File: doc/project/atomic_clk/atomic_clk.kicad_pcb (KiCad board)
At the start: 2 copper layers, 47.8 x 30.2 mm, 22 parts, among them J1 Goldpin, J2 Bat, SW1 POWER, SW2 SET, SW3 CLEAR, U1 BQ-M322RD, U2 STM32F030F4Px, U3 TC1185-3.3VCT8, Y1 18.432MHz

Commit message: better pathm replaced uc
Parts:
- moved U2 9.32 mm to (219.7, 113.5)
- turned R9 to 270 degrees
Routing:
- net D1: track 54.2 -> 24.2 mm
- net D4: track 11.2 -> 38.0 mm, vias 1 -> 0
- net GND: track 97.9 -> 111.3 mm
- net SE: track 32.6 -> 20.3 mm
- net Net-(R8-Pad1): track 37.6 -> 27.9 mm
- net Net-(R9-Pad2): track 30.5 -> 21.3 mm
- net Net-(C1-Pad1): track 19.8 -> 12.0 mm
- net SF: track 42.6 -> 35.7 mm
- net D2: track 23.6 -> 29.9 mm, vias 2 -> 1
- net Net-(C2-Pad1): track 22.5 -> 16.2 mm
- net SB: track 15.1 -> 21.4 mm
- net Net-(SW2-Pad1): track 20.4 -> 14.4 mm
- net SC: track 13.3 -> 19.3 mm
- net SD: track 18.2 -> 12.9 mm
- net +3V3: track 54.3 -> 59.6 mm, vias 2 -> 0
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
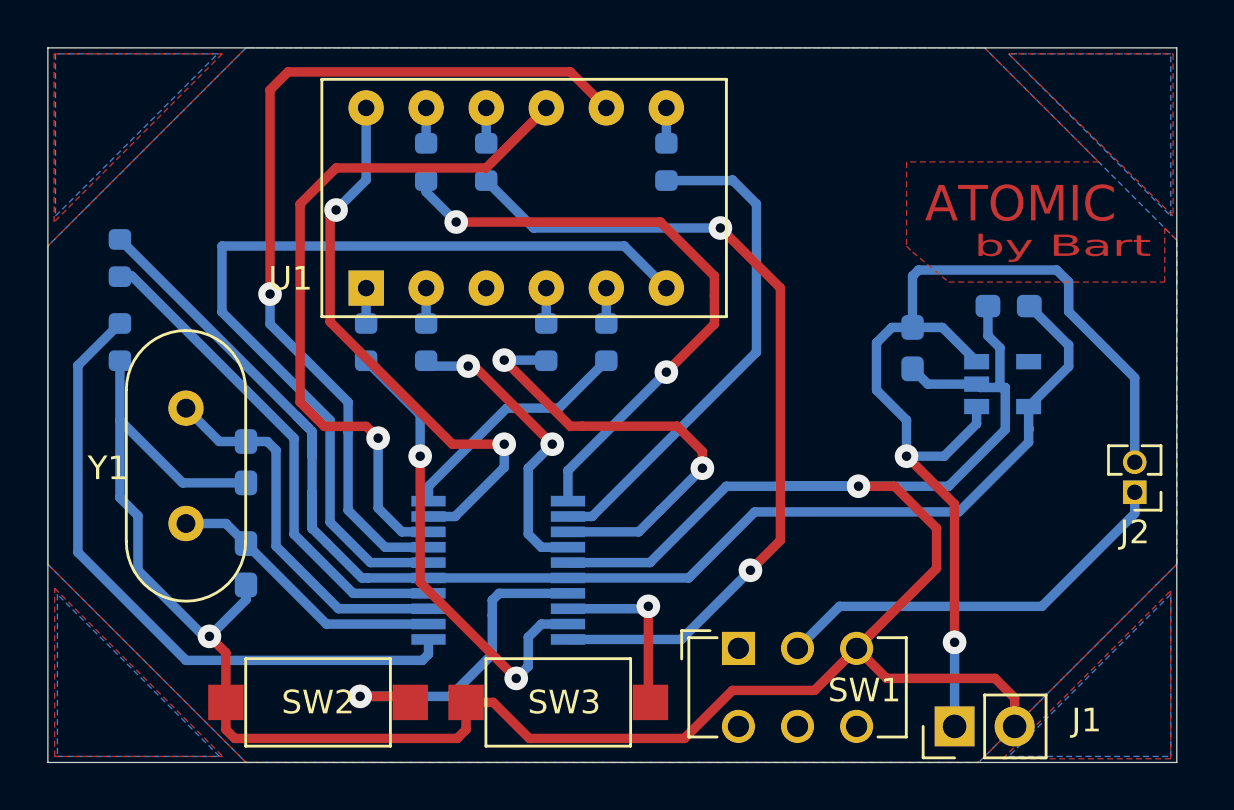
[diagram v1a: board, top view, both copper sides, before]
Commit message: zminimalizowana ilość przelotek
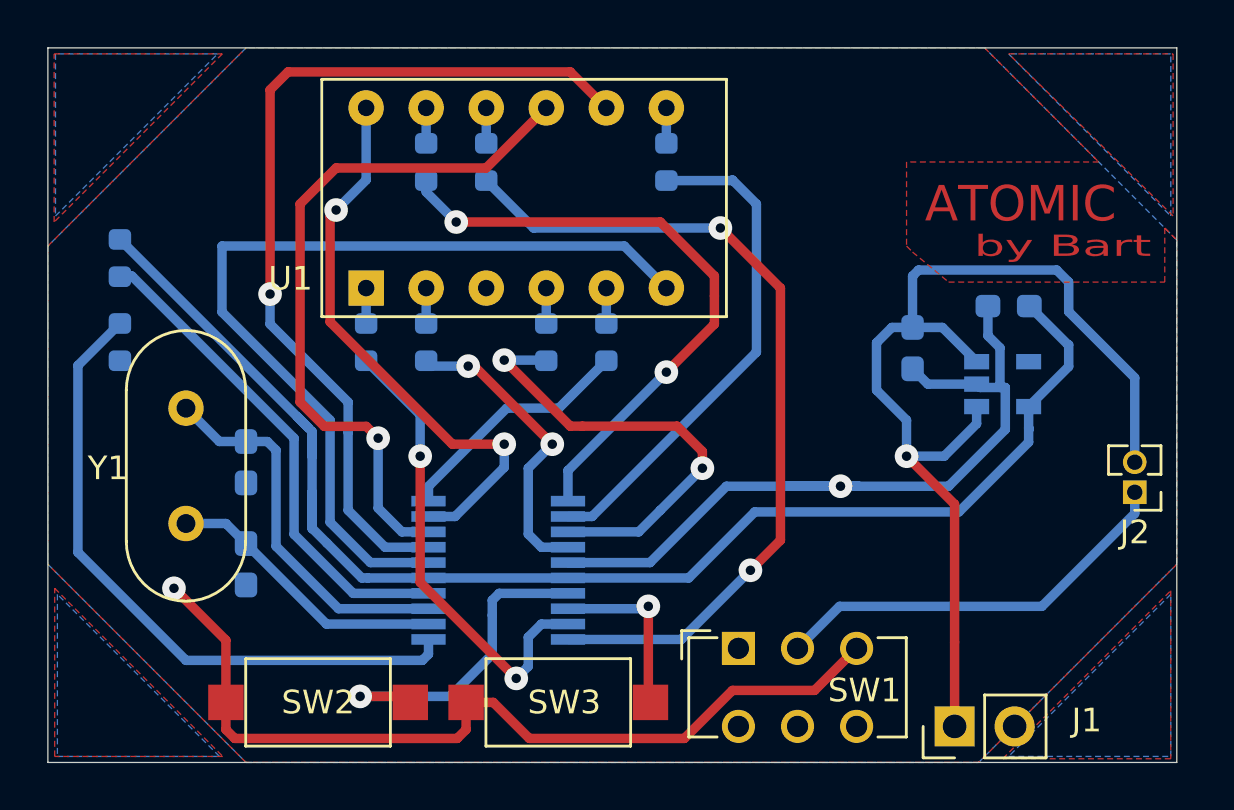
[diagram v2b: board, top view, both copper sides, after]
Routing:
- net GND: track 111.3 -> 71.0 mm
- net Net-(C3-Pad1): vias 2 -> 1

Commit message: correct pads for battery
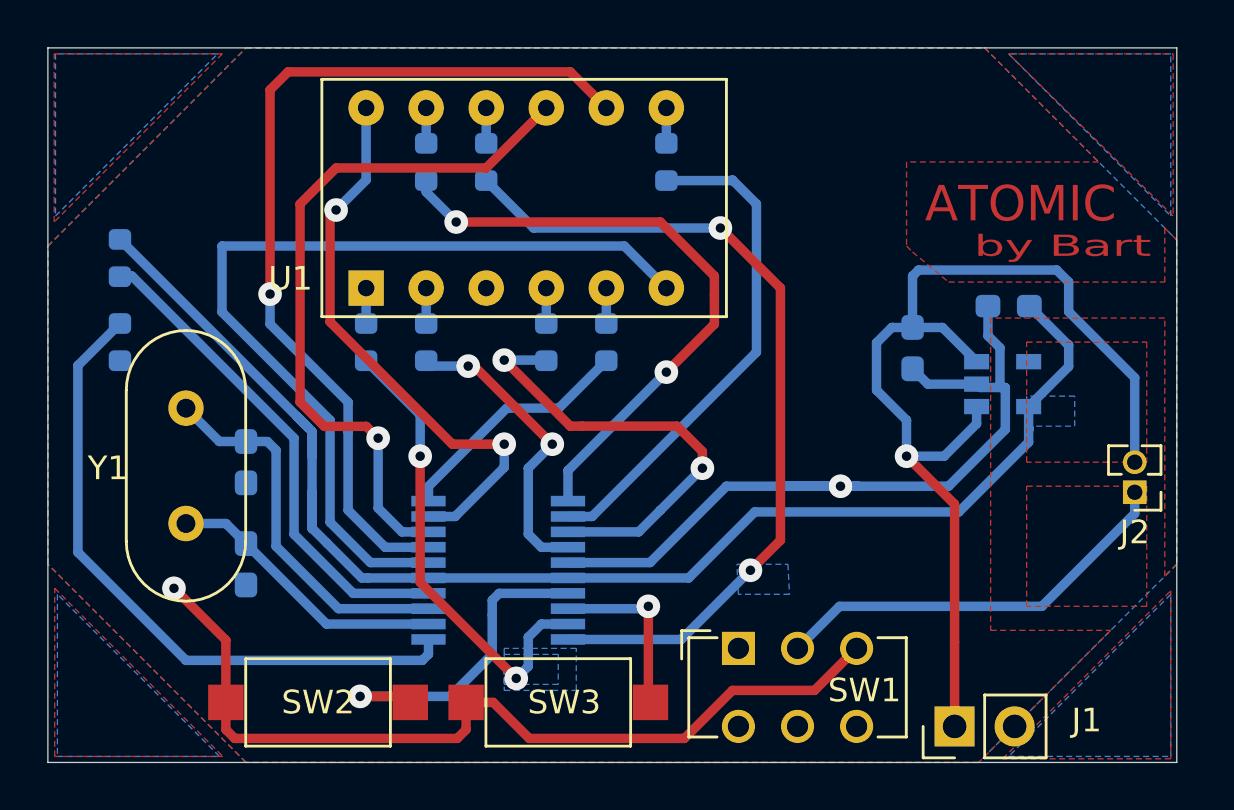
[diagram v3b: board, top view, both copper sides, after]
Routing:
- added copper zone on B.Cu, net +3V3
- added copper zone on F.Cu, net Net-(C3-Pad1)
- added copper zone on F.Cu, net Net-(J2-Pad1)
- added copper zone on B.Cu, net SE
- added copper zone on B.Cu, net SF
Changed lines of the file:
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@@
   (segment (start 242.146 108.12) (end 242.146 107.526) (width 0.4) (layer B.Cu) (net 5))
   (segment (start 242.146 107.526) (end 242.146 106.614) (width 0.4) (layer B.Cu) (net 5))
-  (segment (start 203.9365 101.346) (end 203.708 101.1175) (width 0.4) (layer B.Cu) (net 21))
   (segment (start 243.84 104.92) (end 243.84 103.999) (width 0.4) (layer B.Cu) (net 5))
   (segment (start 242.146 106.614) (end 243.84 104.92) (width 0.4) (layer B.Cu) (net 5))
@@
   (segment (start 206.502 117.348) (end 216.5 117.348) (width 0.4) (layer B.Cu) (net 20))
   (segment (start 216.5 117.348) (end 216.76 117.088) (width 0.4) (layer B.Cu) (net 20))
+  (segment (start 203.9365 101.346) (end 203.708 101.1175) (width 0.4) (layer B.Cu) (net 21))
   (segment (start 216.76 114.513) (end 213.573 114.513) (width 0.4) (layer B.Cu) (net 21))
   (segment (start 211.074 112.014) (end 211.074 107.95) (width 0.4) (layer B.Cu) (net 21))
@@
     )
   )
+  (zone (net 15) (net_name SE) (layer B.Cu) (hatch edge 0.508)
+    (connect_pads (clearance 0.508))
+    (min_thickness 0.254)
+    (fill yes (arc_segments 32) (thermal_gap 0.508) (thermal_bridge_width 0.508))
+    (polygon
+      (pts
+        (xy 219.964 117.602) (xy 219.964 117.094) (xy 222.25 117.094) (xy 222.25 118.364) (xy 219.964 118.364)
+      )
+    )
+  )
+  (zone (net 17) (net_name SF) (layer B.Cu) (hatch edge 0.508)
+    (connect_pads (clearance 0.508))
+    (min_thickness 0.254)
+    (fill yes (arc_segments 32) (thermal_gap 0.508) (thermal_bridge_width 0.508))
+    (polygon
+      (pts
+        (xy 229.8065 113.284) (xy 231.9655 113.284) (xy 232.029 114.554) (xy 229.87 114.554)
+      )
+    )
+  )
+  (zone (net 5) (net_name +3V3) (layer B.Cu) (hatch edge 0.508)
+    (connect_pads (clearance 0.508))
+    (min_thickness 0.254)
+    (fill yes (arc_segments 32) (thermal_gap 0.508) (thermal_bridge_width 0.508))
+    (polygon
+      (pts
+        (xy 242.062 106.172) (xy 242.062 107.442) (xy 244.094 107.442) (xy 244.094 106.172)
+      )
+    )
+  )
+  (zone (net 4) (net_name "Net-(C3-Pad1)") (layer F.Cu) (hatch edge 0.508)
+    (connect_pads (clearance 0.508))
+    (min_thickness 0.254)
+    (fill yes (arc_segments 32) (thermal_gap 0.508) (thermal_bridge_width 0.508))
+    (polygon
+      (pts
+        (xy 247.142 108.966) (xy 242.062 108.966) (xy 242.062 103.886) (xy 247.142 103.886)
+      )
+    )
+  )
+  (zone (net 31) (net_name "Net-(J2-Pad1)") (layer F.Cu) (hatch edge 0.508)
+    (connect_pads (clearance 0.508))
+    (min_thickness 0.254)
+    (fill yes (arc_segments 32) (thermal_gap 0.508) (thermal_bridge_width 0.508))
+    (polygon
+      (pts
+        (xy 247.142 115.062) (xy 242.062 115.062) (xy 242.062 109.982) (xy 247.142 109.982)
+      )
+    )
+  )
+  (zone (net 1) (net_name GND) (layer F.Cu) (hatch edge 0.508)
+    (connect_pads (clearance 0.508))
+    (min_thickness 0.254)
+    (fill yes (arc_segments 32) (thermal_gap 0.508) (thermal_bridge_width 0.508))
+    (polygon
+      (pts
+        (xy 240.538 102.87) (xy 240.538 116.078) (xy 245.618 116.078) (xy 240.03 121.666) (xy 209.042 121.666)
+        (xy 200.66 113.284) (xy 200.66 99.822) (xy 209.042 91.44) (xy 240.284 91.44) (xy 245.11 96.266)
+        (xy 236.982 96.266) (xy 236.982 99.822) (xy 237.236 100.076) (xy 238.76 101.346) (xy 247.904 101.346)
+        (xy 247.904 99.06) (xy 248.412 99.568) (xy 248.412 113.284) (xy 247.904 113.792) (xy 247.904 102.87)
+      )
+    )
+  )
   (zone (net 1) (net_name GND) (layer B.Cu) (hatch edge 0.508)
     (connect_pads (clearance 0.508))
@@
     (polygon
       (pts
-        (xy 209.042 91.44) (xy 200.66 99.822) (xy 200.66 113.284) (xy 209.042 121.666) (xy 240.03 121.666)
-        (xy 248.412 113.284) (xy 248.412 99.568) (xy 240.284 91.44)
-      )
-    )
-  )
-  (zone (net 1) (net_name GND) (layer F.Cu) (hatch edge 0.508)
-    (connect_pads (clearance 0.508))
-    (min_thickness 0.254)
-    (fill yes (arc_segments 32) (thermal_gap 0.508) (thermal_bridge_width 0.508))
-    (polygon
-      (pts
-        (xy 245.11 96.266) (xy 236.982 96.266) (xy 236.982 99.822) (xy 237.236 100.076) (xy 238.76 101.346)
-        (xy 247.904 101.346) (xy 247.904 99.06) (xy 248.412 99.568) (xy 248.412 113.284) (xy 240.03 121.666)
-        (xy 209.042 121.666) (xy 200.66 113.284) (xy 200.66 99.822) (xy 209.042 91.44) (xy 240.284 91.44)
-      )
-    )
+        (xy 248.412 99.568) (xy 248.412 113.284) (xy 240.03 121.666) (xy 209.042 121.666) (xy 200.66 113.284)
+        (xy 200.66 99.822) (xy 209.042 91.44) (xy 240.284 91.44)
+      )
+    )
+    (polygon
+      (pts
+        (xy 219.964 116.84) (xy 219.964 118.618) (xy 223.012 118.618) (xy 223.012 116.84)
+      )
+    )
